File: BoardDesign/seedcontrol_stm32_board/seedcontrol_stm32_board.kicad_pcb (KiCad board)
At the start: 2 copper layers, 90 x 72 mm, 35 parts, among them J1 Input, U1 STM32F401CCUx, U2 MP1584EN

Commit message: Finalized board layout.
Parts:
- added JP1: Programming, Connector_PinHeader_2.54mm:PinHeader_2x05_P2.54mm_Vertical, F.Cu at (153.4, 93.7)
- JI1: value StateInfo/Switches -> Info/Switches
- moved D1 25.1 mm to (106.4, 69.6), turned to 180 degrees
- moved R9 18.1 mm to (133.1, 65.0)
- moved JD1 15.5 mm to (128.8, 87.6)
- moved C2 12.5 mm to (140.2, 78.2)
- moved U1 11.0 mm to (138.0, 73.1)
- moved J1 10.8 mm to (87.4, 55.9), turned to 0 degrees
- moved JS1 9.77 mm to (128.8, 102.1)
- moved R8 9.29 mm to (137.2, 64.8)
- moved R7 8.53 mm to (139.2, 64.8)
- moved R6 7.73 mm to (141.2, 64.8)
- moved JI1 5.45 mm to (134.4, 52.6)
- moved CP1 5.39 mm to (97.7, 85.3)
- moved CP2 5.39 mm to (97.8, 101.3)
- moved CP3 5.39 mm to (97.7, 90.7)
- moved CP5 5.39 mm to (97.7, 80.0)
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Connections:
- U1 pad 34: unconnected-(U1-Pad34) -> Net-(U1-Pad34)
- U1 pad 37: unconnected-(U1-Pad37) -> Net-(U1-Pad37)
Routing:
- net +3.3V: track 0.00 -> 221.0 mm, vias 0 -> 2
- net GND: track 0.00 -> 219.9 mm
- net Net-(CP3-Pad1): track 0.00 -> 102.7 mm
- net Net-(JI1-Pad7): track 0.00 -> 76.4 mm
- net Net-(CP2-Pad1): track 0.00 -> 76.0 mm
- net Net-(CP4-Pad1): track 0.00 -> 68.5 mm
- net Net-(JI1-Pad4): track 0.00 -> 63.7 mm
- net Net-(JI1-Pad6): track 0.00 -> 57.8 mm
- net Net-(CP1-Pad1): track 0.00 -> 56.7 mm
- net Net-(JI1-Pad8): track 0.00 -> 52.0 mm
- net Net-(U1-Pad37): track 0.00 -> 51.9 mm, vias 0 -> 1
- net Net-(JS1-Pad8): track 0.00 -> 45.8 mm
- net Net-(JS1-Pad5): track 0.00 -> 45.7 mm
- net Net-(JS1-Pad7): track 0.00 -> 42.7 mm
- net Net-(CP5-Pad1): track 0.00 -> 41.9 mm
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- added copper zone on B.Cu, net GND
- added copper zone on F.Cu, net GND
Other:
- outline, holes or cut-outs redrawn
- board text added: "12V"
- board text added: "3.3V"
- board text added: "CLK"
- board text added: "Data"
- board text added: "GND"

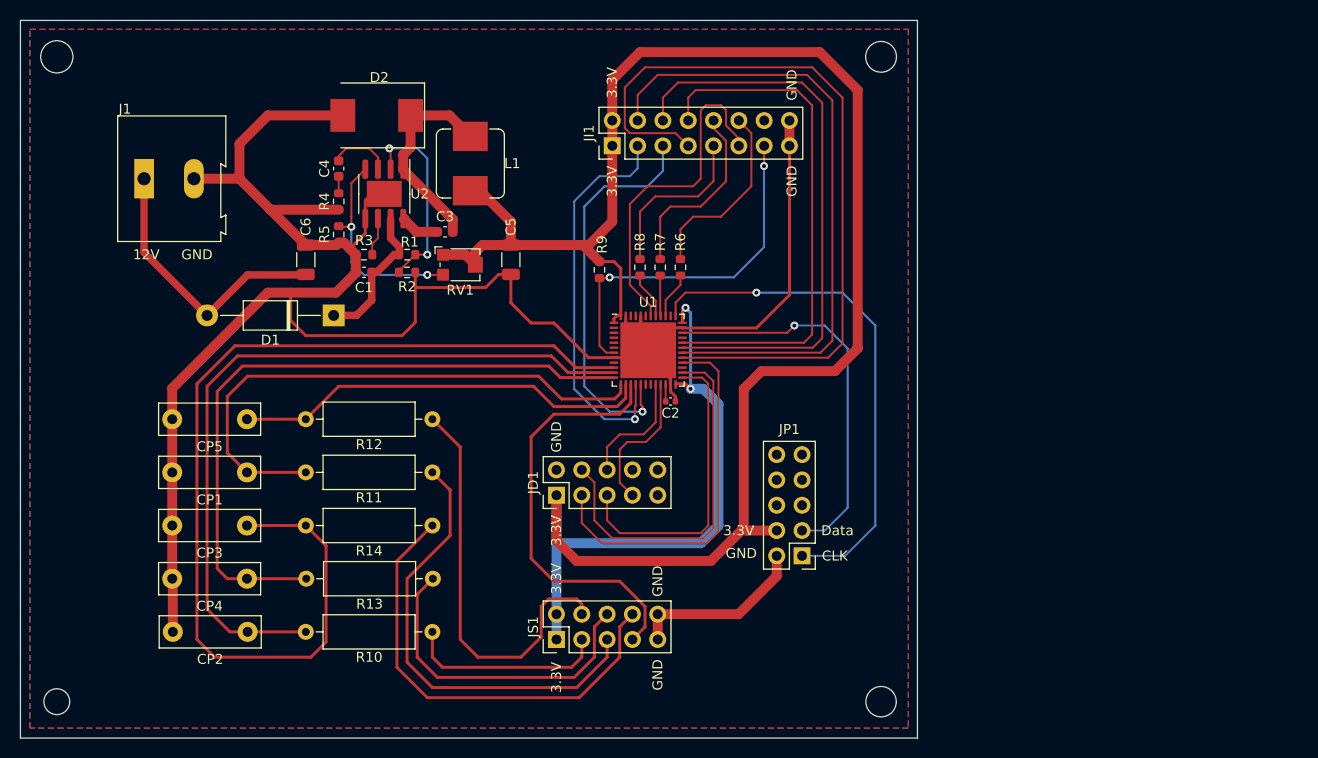
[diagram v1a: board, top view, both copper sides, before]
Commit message: Changed board design. Added footprint for STM32_Blackpill connector.
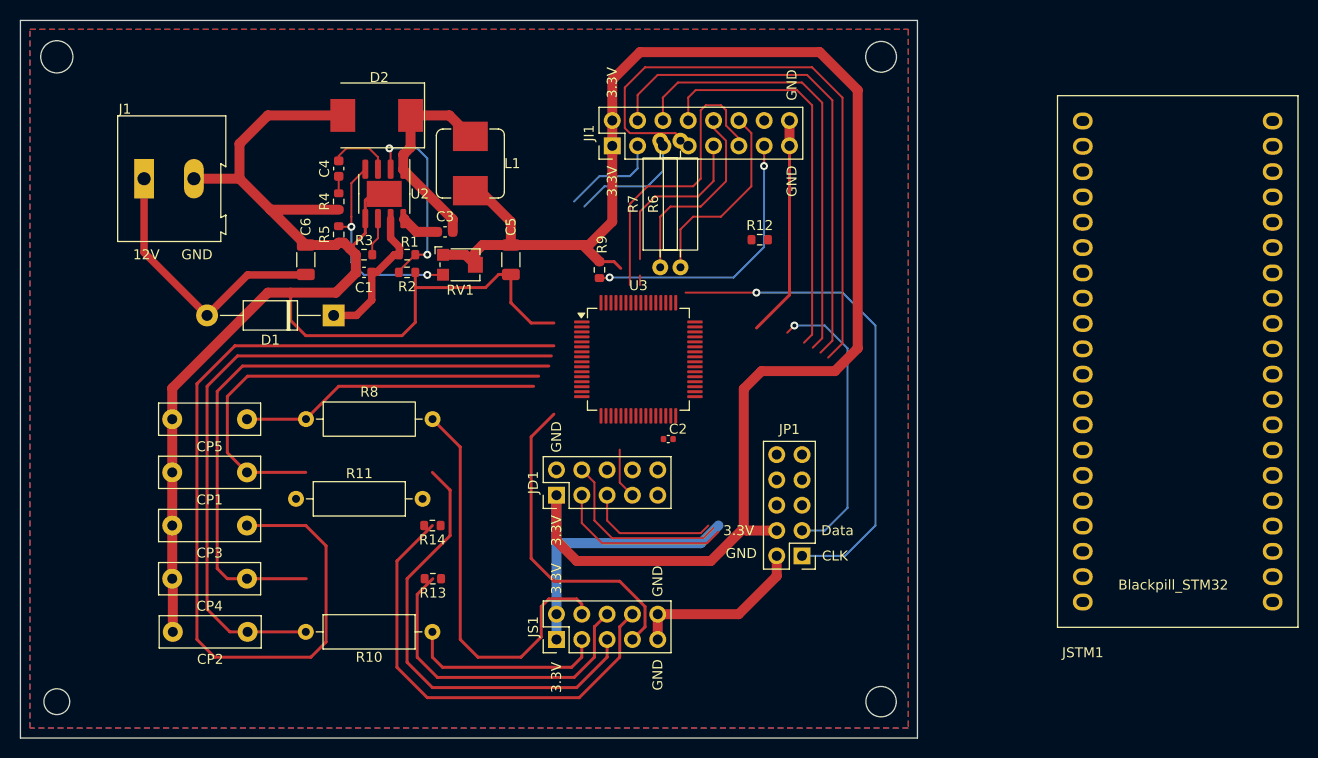
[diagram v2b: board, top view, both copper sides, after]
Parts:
- removed U1: STM32F401CCUx, Package_DFN_QFN:QFN-48-1EP_7x7mm_P0.5mm_EP5.6x5.6mm
- added JSTM1: Conn_02x20_Counter_Clockwise, custom:STM32_Blackpill_header, F.Cu at (181.6, 98.3)
- added U3: STM32F401RCTx, Package_QFP:LQFP-64_10x10mm_P0.5mm, F.Cu at (137.0, 74.0)
- D1: value 1N5408 -> type="D" model="1N5408" lib=""
- R12, R13, R14: footprint Resistor_THT:R_Axial_DIN0309_L9.0mm_D3.2mm_P12.70mm_Horizontal -> Resistor_SMD:R_0603_1608Metric
- R6, R7, R8: footprint Resistor_SMD:R_0603_1608Metric -> Resistor_THT:R_Axial_DIN0309_L9.0mm_D3.2mm_P12.70mm_Horizontal
- moved R12 49.0 mm to (149.2, 62.0)
- moved R8 36.8 mm to (103.7, 80.0), turned to 0 degrees
- moved R11 12.0 mm to (115.3, 88.0), turned to 180 degrees
- moved C2 3.77 mm to (140.0, 82.0)
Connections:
- CP1 pad 1: Net-(CP1-Pad1) -> Net-(U3-PA3)
- CP2 pad 1: Net-(CP2-Pad1) -> Net-(U3-PA1)
- CP3 pad 1: Net-(CP3-Pad1) -> Net-(U3-PA0)
- CP4 pad 1: Net-(CP4-Pad1) -> Net-(U3-PA2)
- CP5 pad 1: Net-(CP5-Pad1) -> Net-(U3-PA4)
- JI1 pad 10: Net-(JI1-Pad10) -> Net-(JI1-Pin_10)
- JI1 pad 12: Net-(JI1-Pad12) -> Net-(JI1-Pin_12)
- JI1 pad 9: Net-(JI1-Pad9) -> Net-(JI1-Pin_9)
- JS1 pad 3: Net-(JS1-Pad3) -> Net-(JS1-Pin_3)
- JS1 pad 4: Net-(JS1-Pad4) -> Net-(JS1-Pin_4)
- JS1 pad 5: Net-(JS1-Pad5) -> Net-(JS1-Pin_5)
- JS1 pad 6: Net-(JS1-Pad6) -> Net-(JS1-Pin_6)
- JS1 pad 8: Net-(JS1-Pad8) -> Net-(JS1-Pin_8)
- R10 pad 1: Net-(CP2-Pad1) -> Net-(JS1-Pin_6)
- R10 pad 2: Net-(JS1-Pad3) -> Net-(U3-PA2)
- R11 pad 1: Net-(CP1-Pad1) -> Net-(JS1-Pin_8)
- R11 pad 2: Net-(JS1-Pad5) -> Net-(U3-PA0)
- R12 pad 1: Net-(CP5-Pad1) -> Net-(U3-PB3)
- R12 pad 2: Net-(JS1-Pad4) -> Net-(JI1-Pin_12)
- R13 pad 1: Net-(JS1-Pad6) -> Net-(U3-PB4)
- R13 pad 2: Net-(CP4-Pad1) -> Net-(JI1-Pin_10)
- R14 pad 1: Net-(JS1-Pad8) -> Net-(JI1-Pin_9)
- R14 pad 2: Net-(CP3-Pad1) -> Net-(U3-PB5)
- R6 pad 1: Net-(R6-Pad1) -> Net-(U3-PA1)
- R6 pad 2: Net-(JI1-Pad12) -> Net-(JS1-Pin_3)
- R7 pad 1: Net-(R7-Pad1) -> Net-(U3-PA3)
- R7 pad 2: Net-(JI1-Pad10) -> Net-(JS1-Pin_5)
- R8 pad 1: Net-(R8-Pad1) -> Net-(U3-PA4)
- R8 pad 2: Net-(JI1-Pad9) -> Net-(JS1-Pin_4)
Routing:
- net (no net): track 0.00 -> 280.4 mm
- net Net-(CP3-Pad1): track 102.7 -> 0.00 mm
- net Net-(U3-PA0): track 0.00 -> 95.8 mm
- net Net-(JI1-Pin_7): track 76.4 -> 0.00 mm
- net Net-(CP2-Pad1): track 76.0 -> 0.00 mm
- net Net-(CP4-Pad1): track 68.5 -> 0.00 mm
- net Net-(U3-PA2): track 0.00 -> 61.5 mm
- net Net-(CP1-Pad1): track 56.7 -> 0.00 mm
- net Net-(U3-PA3): track 0.00 -> 46.4 mm
- net Net-(JS1-Pad8): track 45.8 -> 0.00 mm
- net Net-(JS1-Pin_5): track 0.00 -> 45.7 mm
- net Net-(JS1-Pad5): track 45.7 -> 0.00 mm
- net Net-(CP5-Pad1): track 41.9 -> 0.00 mm
- net Net-(JS1-Pin_4): track 0.00 -> 41.6 mm
- net Net-(JS1-Pad4): track 41.6 -> 0.00 mm
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
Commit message: Finalized schematics. Placed all components in Boardview.
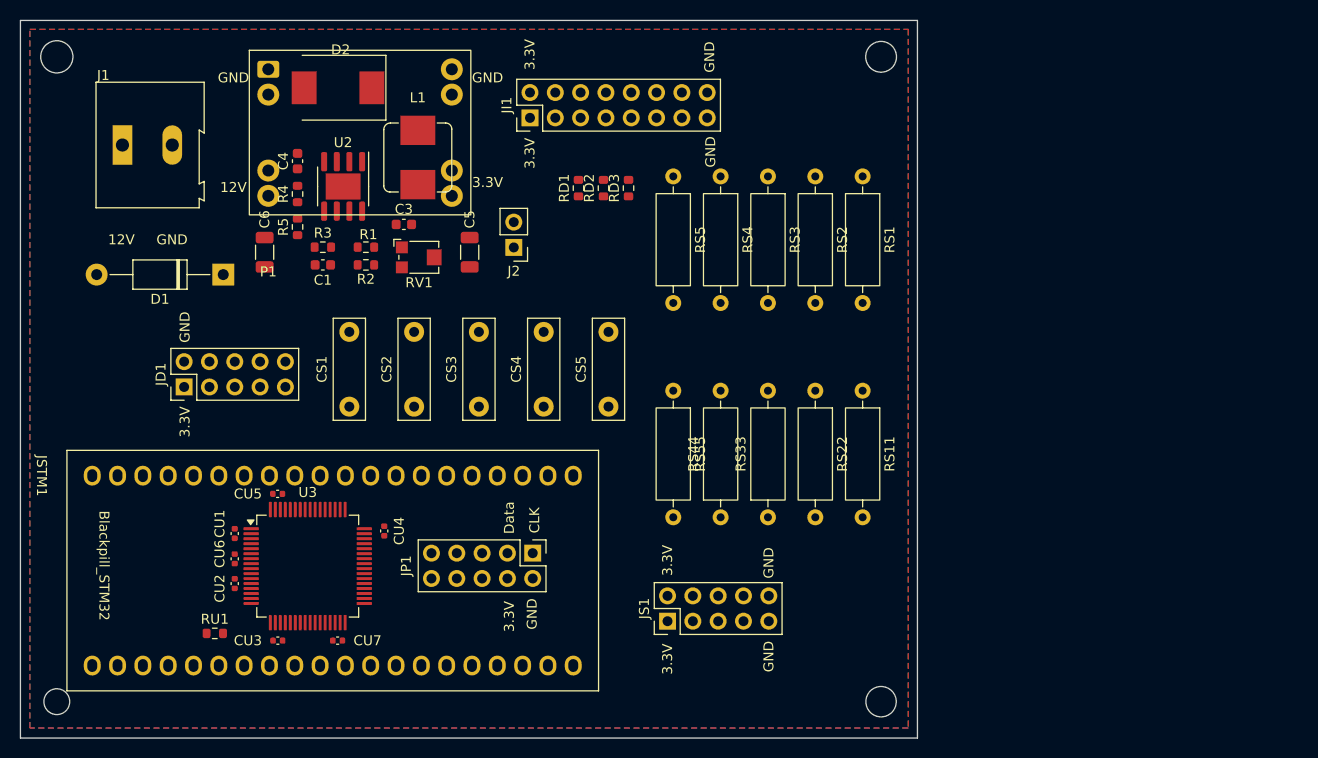
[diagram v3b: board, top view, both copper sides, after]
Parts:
- removed C2: 2.2µF, Capacitor_SMD:C_0402_1005Metric
- removed CP1, CP2, CP3, CP4, CP5: 1µF, Capacitor_THT:C_Rect_L10.0mm_W3.0mm_P7.50mm_MKS4
- removed R10, R11, R6, R7, R8: R, Resistor_THT:R_Axial_DIN0309_L9.0mm_D3.2mm_P12.70mm_Horizontal
- removed R12, R13, R14, R9: R, Resistor_SMD:R_0603_1608Metric
- added CS1: 1µF, Capacitor_THT:C_Rect_L10.0mm_W3.0mm_P7.50mm_MKS4, F.Cu at (108.0, 78.8)
- added CS2: 1µF, Capacitor_THT:C_Rect_L10.0mm_W3.0mm_P7.50mm_MKS4, F.Cu at (114.5, 78.8)
- added CS3: 1µF, Capacitor_THT:C_Rect_L10.0mm_W3.0mm_P7.50mm_MKS4, F.Cu at (121.0, 78.8)
- added CS4: 1µF, Capacitor_THT:C_Rect_L10.0mm_W3.0mm_P7.50mm_MKS4, F.Cu at (127.5, 78.8)
- added CS5: 1µF, Capacitor_THT:C_Rect_L10.0mm_W3.0mm_P7.50mm_MKS4, F.Cu at (134.0, 78.8)
- added CU1: 100nF, Capacitor_SMD:C_0402_1005Metric, F.Cu at (96.5, 91.5)
- added CU2: 100nF, Capacitor_SMD:C_0402_1005Metric, F.Cu at (96.5, 96.5)
- added CU3: 100nF, Capacitor_SMD:C_0402_1005Metric, F.Cu at (100.8, 102.2)
- added CU4: 100nF, Capacitor_SMD:C_0402_1005Metric, F.Cu at (111.5, 91.2)
- added CU5: 100nF, Capacitor_SMD:C_0402_1005Metric, F.Cu at (100.8, 87.5)
- added CU6: 100nF, Capacitor_SMD:C_0402_1005Metric, F.Cu at (96.5, 94.0)
- added CU7: 2.2µF, Capacitor_SMD:C_0402_1005Metric, F.Cu at (106.8, 102.2)
- added J2: Conn_01x02_Pin, Connector_PinHeader_2.54mm:PinHeader_1x02_P2.54mm_Vertical, F.Cu at (124.5, 62.8)
- added P1: ~, custom:Voltage_converter, F.Cu at (99.9, 57.6)
- added RD1: R, Resistor_SMD:R_0603_1608Metric, F.Cu at (131.0, 56.8)
- added RD2: R, Resistor_SMD:R_0603_1608Metric, F.Cu at (133.5, 56.8)
- added RD3: R, Resistor_SMD:R_0603_1608Metric, F.Cu at (136.0, 56.8)
- added RS1: 4,7k, Resistor_THT:R_Axial_DIN0309_L9.0mm_D3.2mm_P12.70mm_Horizontal, F.Cu at (159.5, 55.6)
- added RS11: 150, Resistor_THT:R_Axial_DIN0309_L9.0mm_D3.2mm_P12.70mm_Horizontal, F.Cu at (159.5, 77.2)
- added RS2: 4,7k, Resistor_THT:R_Axial_DIN0309_L9.0mm_D3.2mm_P12.70mm_Horizontal, F.Cu at (154.8, 55.6)
- added RS22: 150, Resistor_THT:R_Axial_DIN0309_L9.0mm_D3.2mm_P12.70mm_Horizontal, F.Cu at (154.8, 77.2)
- added RS3: 4,7k, Resistor_THT:R_Axial_DIN0309_L9.0mm_D3.2mm_P12.70mm_Horizontal, F.Cu at (150.0, 55.6)
- added RS33: 150, Resistor_THT:R_Axial_DIN0309_L9.0mm_D3.2mm_P12.70mm_Horizontal, F.Cu at (150.0, 89.8)
- added RS4: 4,7k, Resistor_THT:R_Axial_DIN0309_L9.0mm_D3.2mm_P12.70mm_Horizontal, F.Cu at (145.2, 55.6)
- added RS44: 150, Resistor_THT:R_Axial_DIN0309_L9.0mm_D3.2mm_P12.70mm_Horizontal, F.Cu at (145.2, 89.8)
- added RS5: 4,7k, Resistor_THT:R_Axial_DIN0309_L9.0mm_D3.2mm_P12.70mm_Horizontal, F.Cu at (140.5, 55.6)
- added RS55: 150, Resistor_THT:R_Axial_DIN0309_L9.0mm_D3.2mm_P12.70mm_Horizontal, F.Cu at (140.5, 77.2)
- added RU1: R, Resistor_SMD:R_0603_1608Metric, F.Cu at (94.5, 101.5)
- D1: value type="D" model="1N5408" lib="" -> ~
- moved JSTM1 100.2 mm to (82.2, 85.7), turned to -90 degrees
- moved U3 39.1 mm to (103.8, 94.8)
- moved JD1 38.9 mm to (91.4, 76.8)
- moved JP1 27.0 mm to (126.4, 93.5), turned to -90 degrees
- moved D1 11.8 mm to (95.3, 65.5)
- moved JS1 11.3 mm to (139.9, 100.3)
- moved JI1 8.72 mm to (126.1, 49.8)
- moved L1 5.31 mm to (114.9, 53.8)
- moved D2 4.77 mm to (106.9, 46.8)
- moved C1 4.20 mm to (105.3, 64.5)
- moved R2 4.20 mm to (109.7, 64.5)
- moved R1 4.20 mm to (109.7, 62.8)
- moved R3 4.20 mm to (105.3, 62.8)
- moved R5 4.20 mm to (102.8, 60.7)
- moved RV1 4.20 mm to (115.1, 63.8)
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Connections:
- net Net-(JP1-Pin_1) renamed /PA14
- net Net-(JP1-Pin_3) renamed /PA13
- C5 pad 2: +3.3V -> /3,3V
- JD1 pad 3: Net-(JD1-Pin_3) -> /PB15
- JD1 pad 4: Net-(JD1-Pin_4) -> /PB13
- JD1 pad 5: Net-(JD1-Pin_5) -> /PB12
- JD1 pad 6: Net-(JD1-Pin_6) -> /PB2
- JD1 pad 7: Net-(JD1-Pin_7) -> /PB10
- JI1 pad 11: Net-(JI1-Pin_11) -> /PB6
- JI1 pad 13: Net-(JI1-Pin_13) -> /RESET
- JI1 pad 3: Net-(JI1-Pin_3) -> /PA6
- JI1 pad 4: Net-(JI1-Pin_4) -> /PA9
- JI1 pad 5: Net-(JI1-Pin_5) -> /PA7
- JI1 pad 6: Net-(JI1-Pin_6) -> /PA10
- JI1 pad 7: Net-(JI1-Pin_7) -> /PA8
- JI1 pad 8: Net-(JI1-Pin_8) -> /PA11
- JS1 pad 7: Net-(JS1-Pin_7) -> /PA5
- JSTM1 pad 1: unconnected-(JSTM1-Pin_1-Pad1) -> /PB12
- JSTM1 pad 10: unconnected-(JSTM1-Pin_10-Pad10) -> /PA15
- JSTM1 pad 11: unconnected-(JSTM1-Pin_11-Pad11) -> /PB3
- JSTM1 pad 12: unconnected-(JSTM1-Pin_12-Pad12) -> /PB4
- JSTM1 pad 13: unconnected-(JSTM1-Pin_13-Pad13) -> /PB5
- JSTM1 pad 14: unconnected-(JSTM1-Pin_14-Pad14) -> /PB6
- JSTM1 pad 15: unconnected-(JSTM1-Pin_15-Pad15) -> /PB7
- JSTM1 pad 16: unconnected-(JSTM1-Pin_16-Pad16) -> /PB8
- JSTM1 pad 17: unconnected-(JSTM1-Pin_17-Pad17) -> /PB9
- JSTM1 pad 2: unconnected-(JSTM1-Pin_2-Pad2) -> /PB13
- JSTM1 pad 21: unconnected-(JSTM1-Pin_21-Pad21) -> +3.3V
- JSTM1 pad 22: unconnected-(JSTM1-Pin_22-Pad22) -> /PC13
- JSTM1 pad 23: unconnected-(JSTM1-Pin_23-Pad23) -> /PC14
- JSTM1 pad 24: unconnected-(JSTM1-Pin_24-Pad24) -> /PC15
- JSTM1 pad 25: unconnected-(JSTM1-Pin_25-Pad25) -> /RESET
- JSTM1 pad 26: unconnected-(JSTM1-Pin_26-Pad26) -> /PA0
- JSTM1 pad 27: unconnected-(JSTM1-Pin_27-Pad27) -> /PA1
- JSTM1 pad 28: unconnected-(JSTM1-Pin_28-Pad28) -> /PA2
- JSTM1 pad 29: unconnected-(JSTM1-Pin_29-Pad29) -> /PA3
- JSTM1 pad 3: unconnected-(JSTM1-Pin_3-Pad3) -> /PB14
- JSTM1 pad 30: unconnected-(JSTM1-Pin_30-Pad30) -> /PA4
- JSTM1 pad 31: unconnected-(JSTM1-Pin_31-Pad31) -> /PA5
- JSTM1 pad 32: unconnected-(JSTM1-Pin_32-Pad32) -> /PA6
- JSTM1 pad 33: unconnected-(JSTM1-Pin_33-Pad33) -> /PA7
- JSTM1 pad 34: unconnected-(JSTM1-Pin_34-Pad34) -> /PB0
- JSTM1 pad 35: unconnected-(JSTM1-Pin_35-Pad35) -> /PB1
- JSTM1 pad 36: unconnected-(JSTM1-Pin_36-Pad36) -> /PB2
- JSTM1 pad 37: unconnected-(JSTM1-Pin_37-Pad37) -> /PB10
- JSTM1 pad 4: unconnected-(JSTM1-Pin_4-Pad4) -> /PB15
- JSTM1 pad 5: unconnected-(JSTM1-Pin_5-Pad5) -> /PA8
- JSTM1 pad 6: unconnected-(JSTM1-Pin_6-Pad6) -> /PA9
- JSTM1 pad 7: unconnected-(JSTM1-Pin_7-Pad7) -> /PA10
- JSTM1 pad 8: unconnected-(JSTM1-Pin_8-Pad8) -> /PA11
- JSTM1 pad 9: unconnected-(JSTM1-Pin_9-Pad9) -> /PA12
- L1 pad 2: +3.3V -> /3,3V
- RV1 pad 1: +3.3V -> /3,3V
- RV1 pad 2: +3.3V -> /3,3V
- U3 pad 13: unconnected-(U3-VREF+-Pad13) -> +3.3V
- U3 pad 14: Net-(U3-PA0) -> /PA0
- U3 pad 15: Net-(U3-PA1) -> /PA1
- U3 pad 16: Net-(U3-PA2) -> /PA2
- U3 pad 17: Net-(U3-PA3) -> /PA3
- U3 pad 2: unconnected-(U3-PC13-Pad2) -> /PC13
- U3 pad 20: Net-(U3-PA4) -> /PA4
- U3 pad 21: Net-(JS1-Pin_7) -> /PA5
- U3 pad 22: Net-(JI1-Pin_3) -> /PA6
- U3 pad 23: Net-(JI1-Pin_5) -> /PA7
- U3 pad 26: unconnected-(U3-PB0-Pad26) -> /PB0
- U3 pad 27: unconnected-(U3-PB1-Pad27) -> /PB1
- U3 pad 28: Net-(JD1-Pin_6) -> /PB2
- U3 pad 29: Net-(JD1-Pin_7) -> /PB10
- U3 pad 3: unconnected-(U3-PC14-Pad3) -> /PC14
- U3 pad 33: Net-(JD1-Pin_5) -> /PB12
- U3 pad 34: Net-(JD1-Pin_4) -> /PB13
- U3 pad 35: unconnected-(U3-PB14-Pad35) -> /PB14
- U3 pad 36: Net-(JD1-Pin_3) -> /PB15
- U3 pad 4: unconnected-(U3-PC15-Pad4) -> /PC15
- U3 pad 41: Net-(JI1-Pin_7) -> /PA8
- U3 pad 42: Net-(JI1-Pin_4) -> /PA9
- U3 pad 43: Net-(JI1-Pin_6) -> /PA10
- U3 pad 44: Net-(JI1-Pin_8) -> /PA11
- U3 pad 45: unconnected-(U3-PA12-Pad45) -> /PA12
- U3 pad 50: unconnected-(U3-PA15-Pad50) -> /PA15
- U3 pad 55: Net-(U3-PB3) -> /PB3
- U3 pad 56: Net-(U3-PB4) -> /PB4
- U3 pad 57: Net-(U3-PB5) -> /PB5
- U3 pad 58: Net-(JI1-Pin_11) -> /PB6
- U3 pad 59: unconnected-(U3-PB7-Pad59) -> /PB7
- U3 pad 61: unconnected-(U3-PB8-Pad61) -> /PB8
- U3 pad 62: unconnected-(U3-PB9-Pad62) -> /PB9
- U3 pad 7: Net-(JI1-Pin_13) -> /RESET
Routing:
- net (no net): track 280.4 -> 0.00 mm
- net +3.3V: track 187.4 -> 0.00 mm
- net GND: track 178.7 -> 0.00 mm
- net Net-(U3-PA0): track 95.8 -> 0.00 mm
- net Net-(U3-PA2): track 61.5 -> 0.00 mm
- net Net-(JI1-Pin_4): track 49.8 -> 0.00 mm
- net /PA14: track 49.1 -> 0.00 mm, vias 1 -> 0
- net Net-(U3-PA3): track 46.4 -> 0.00 mm
- net Net-(JS1-Pin_5): track 45.7 -> 0.00 mm
- net Net-(JI1-Pin_6): track 44.7 -> 0.00 mm
- net Net-(JS1-Pin_4): track 41.6 -> 0.00 mm
- net Net-(JI1-Pin_8): track 39.8 -> 0.00 mm
- net Net-(JS1-Pin_7): track 32.7 -> 0.00 mm
- net Net-(JI1-Pin_11): track 30.2 -> 0.00 mm
- net Net-(U3-PA4): track 30.1 -> 0.00 mm
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
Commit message: Final Board design.
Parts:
- D2: footprint Diode_SMD:D_SMC -> Diode_SMD:D_SMA
- RS1, RS2, RS3, RS4, RS5: value 4,7k -> 4,7-10k
- RV1: value R_Potentiometer -> R_Pot
- moved CU5 15.8 mm to (109.0, 101.0)
- moved D1 12.2 mm to (83.2, 66.5), turned to 0 degrees
- moved JP1 10.7 mm to (137.1, 94.2)
- moved JS1 6.36 mm to (144.4, 95.8)
- moved RD1 5.70 mm to (129.5, 62.3), turned to -90 degrees
- moved RD2 5.59 mm to (132.5, 62.3)
- moved RD3 5.52 mm to (135.5, 62.3)
- moved RS11 4.15 mm to (159.5, 73.0)
- moved RS22 4.15 mm to (154.8, 73.0)
- moved RS55 4.15 mm to (140.5, 73.0)
- moved RS33 4.15 mm to (150.0, 85.7)
- moved RS44 4.15 mm to (145.2, 85.7)
- moved CU1 2.90 mm to (98.0, 89.0), turned to -90 degrees
- moved L1 1.95 mm to (114.0, 52.0)
- moved JI1 1.75 mm to (127.9, 49.8)
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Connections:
- net /3,3V renamed /V3,3
- C1 pad 2: Net-(D1-A) -> /V12
- C6 pad 2: +12V -> /V12
- D1 pad 1: Net-(D1-A) -> +12V
- D1 pad 2: +12V -> /V12
- P1 pad 3: +12V -> /V12
- P1 pad 4: +12V -> /V12
- R1 pad 2: Net-(D1-A) -> /V12
- U2 pad 7: Net-(D1-A) -> /V12
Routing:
- net +3.3V: track 0.00 -> 377.1 mm, vias 0 -> 1
- net GND: track 0.00 -> 179.5 mm, vias 0 -> 2
- net /PA3: track 0.00 -> 176.5 mm, vias 0 -> 1
- net /PA1: track 0.00 -> 152.1 mm, vias 0 -> 1
- net /RESET: track 0.00 -> 150.3 mm
- net /PA6: track 0.00 -> 135.0 mm, vias 0 -> 1
- net /PA0: track 0.00 -> 131.1 mm
- net /PA7: track 0.00 -> 123.6 mm, vias 0 -> 2
- net /PA2: track 0.00 -> 109.1 mm
- net /PA4: track 0.00 -> 82.4 mm
- net /PB6: track 0.00 -> 77.3 mm, vias 0 -> 2
- net /PA9: track 0.00 -> 73.5 mm, vias 0 -> 1
- net /PA10: track 0.00 -> 69.7 mm, vias 0 -> 1
- net /PB12: track 0.00 -> 68.7 mm
- net /PB13: track 0.00 -> 68.7 mm
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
